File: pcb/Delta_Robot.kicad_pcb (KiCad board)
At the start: 2 copper layers, 95.5 x 69.6 mm, 136 parts, among them IC1 STMPS2151STR, J1 Conn_01x04, J2 Conn_01x03, J3 USB_A, J4 Conn_01x02, J5 Conn_01x02, J6 MP3V5050VC6U, J7 RJ45, J8 USB_OTG, J9 Conn_01x03, Q1 IRF9540STRLPBF, Q2 IRF9540STRLPBF, SW3 TL3305A, SW4 TL3305A, U2 LDL1117S33R, U3 ZLDO1117G12TA, U4 ICE40UP5K-SG48I, U5 W25Q64JVSSIQ, U6 STM32F412RGT6, U7 Omega2+, U8 4N25-X007T, U9 4N25-X007T, Y1 8MHz, Y2 32.768KHZ

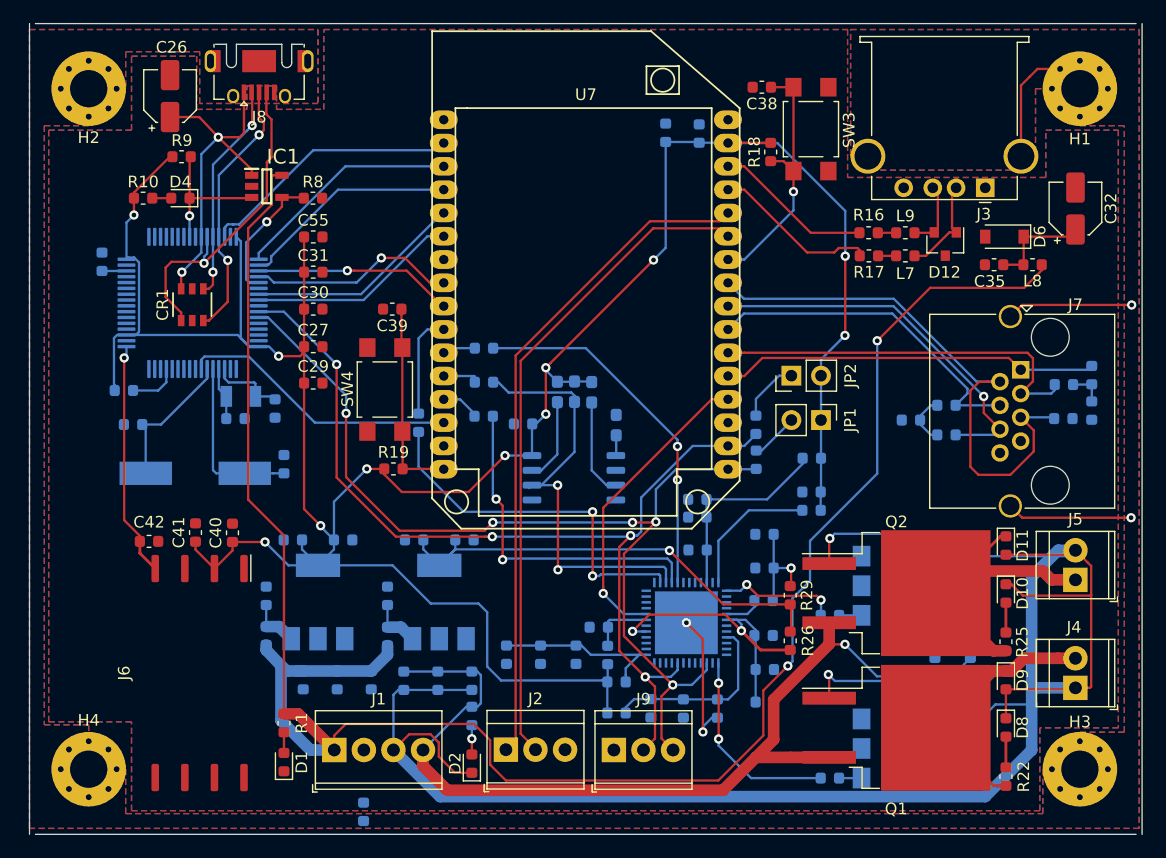
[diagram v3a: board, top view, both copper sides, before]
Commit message: Mejora footprint USB-A-B
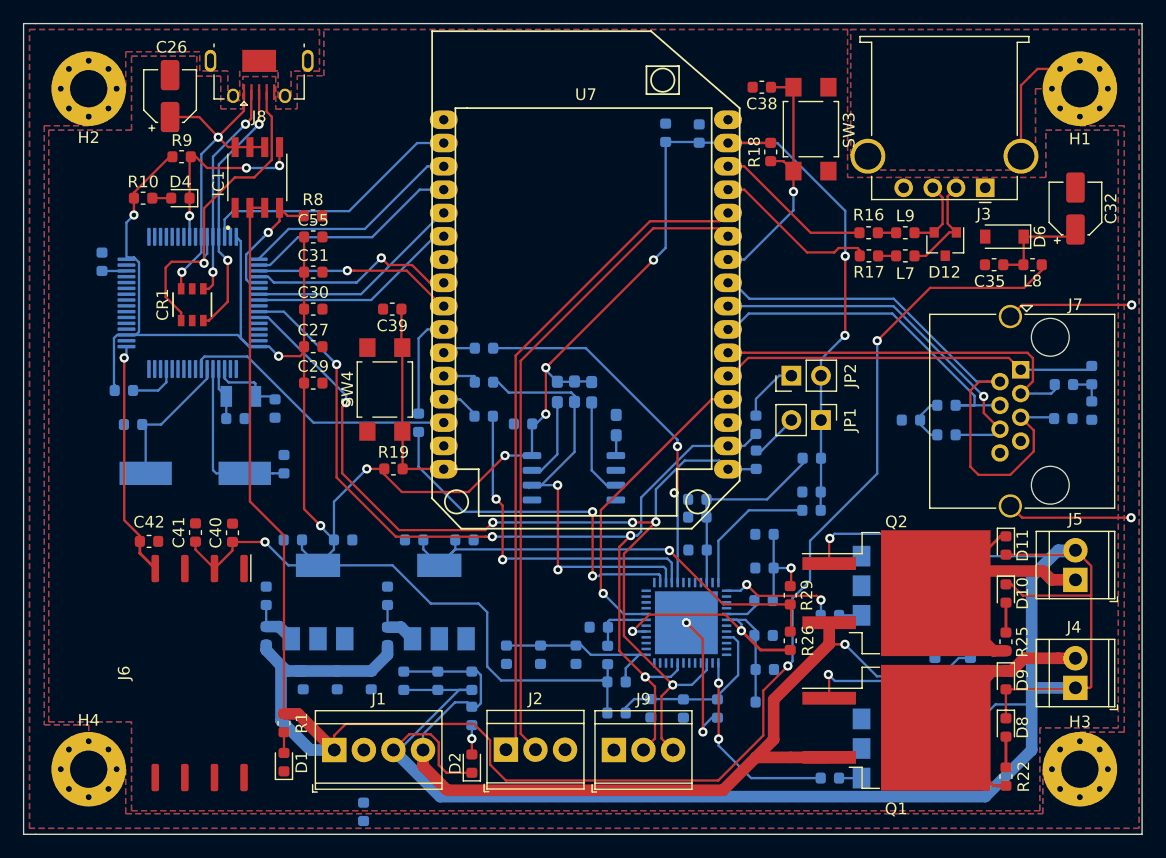
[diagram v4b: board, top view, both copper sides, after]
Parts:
- IC1: value STMPS2151STR -> STMPS2151MTR; footprint SMD:SOT95P280X145-5N -> SMD:SOIC127P600X175-8N
- J8: footprint Connector_USB:USB_Micro-AB_Molex_47590-0001 -> SMD:USB_Micro-AB_Molex_47590-0001
- moved R8 1.52 mm to (114.5, 73.2)
- moved IC1 1.11 mm to (109.7, 69.8), turned to 90 degrees
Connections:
- IC1 pad 1: /STM32/STM32_USB_VBUS -> GND
- IC1 pad 2: GND -> +5V
- IC1 pad 3: /STM32/STM32_USB_OverCurrent -> +5V
- IC1 pad 5: +5V -> /STM32/STM32_USB_OverCurrent
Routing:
- net /STM32/STM32_USB_OverCurrent: track 12.9 -> 17.2 mm, vias 1 -> 3
- net GNDPWR: track 153.6 -> 157.1 mm
- net +5V: track 177.4 -> 174.1 mm
- net Net-(Q1-Pad1): track 21.8 -> 23.9 mm
- net /Onion Omega 2/OMEGA2_ETH_TX+: track 29.5 -> 30.9 mm
- net /STM32/STM32_USB_VBUS: track 29.6 -> 28.4 mm
- net +24V: track 82.1 -> 83.2 mm
- net /External Communications/EXT_I2C1: track 85.5 -> 86.4 mm
- net /STM32/STM32_USB_ID: track 28.5 -> 29.3 mm
- net /FPGA/FPGA_VCCIO_O: track 16.1 -> 15.6 mm
- net /STM32/STM32_USB_PowerSwitchOn: track 11.4 -> 10.9 mm
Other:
- board size 95.5 x 69.6 mm -> 96 x 69.6 mm

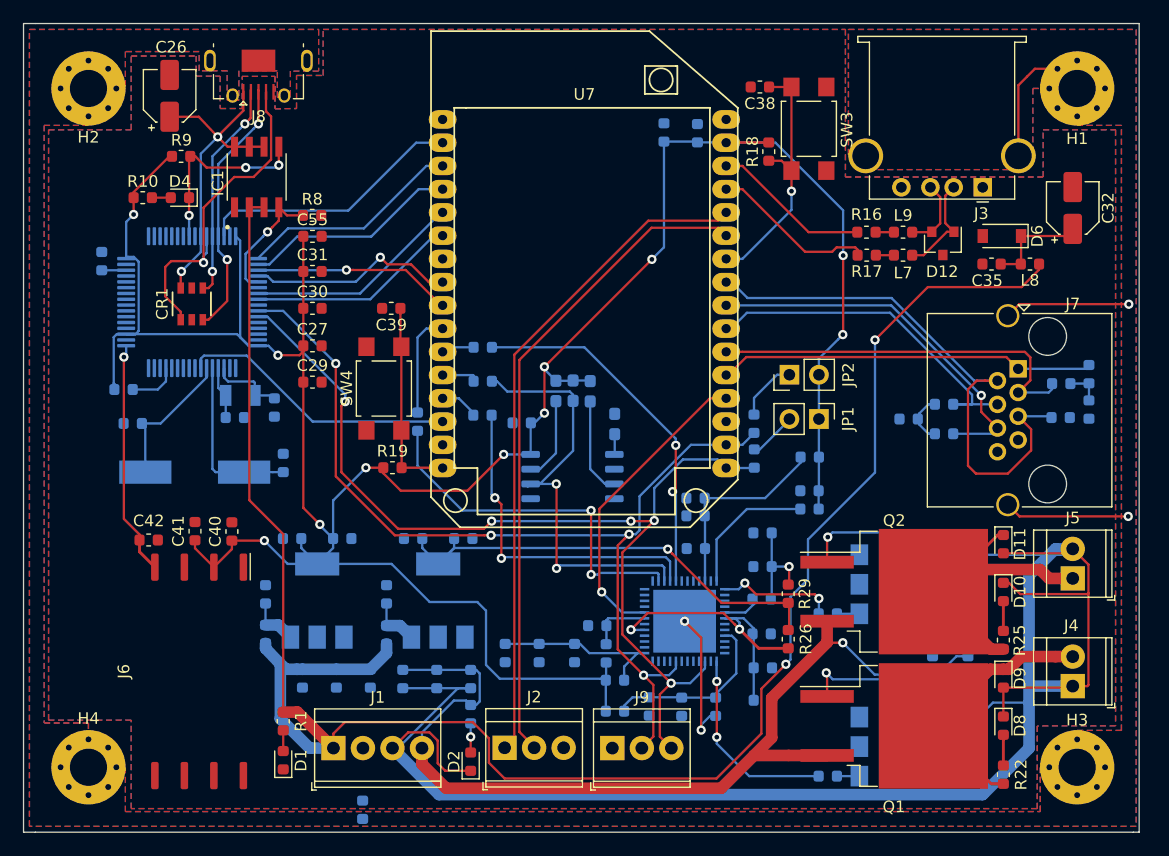
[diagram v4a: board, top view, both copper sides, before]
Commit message: Correccion UART Micro-Omega2
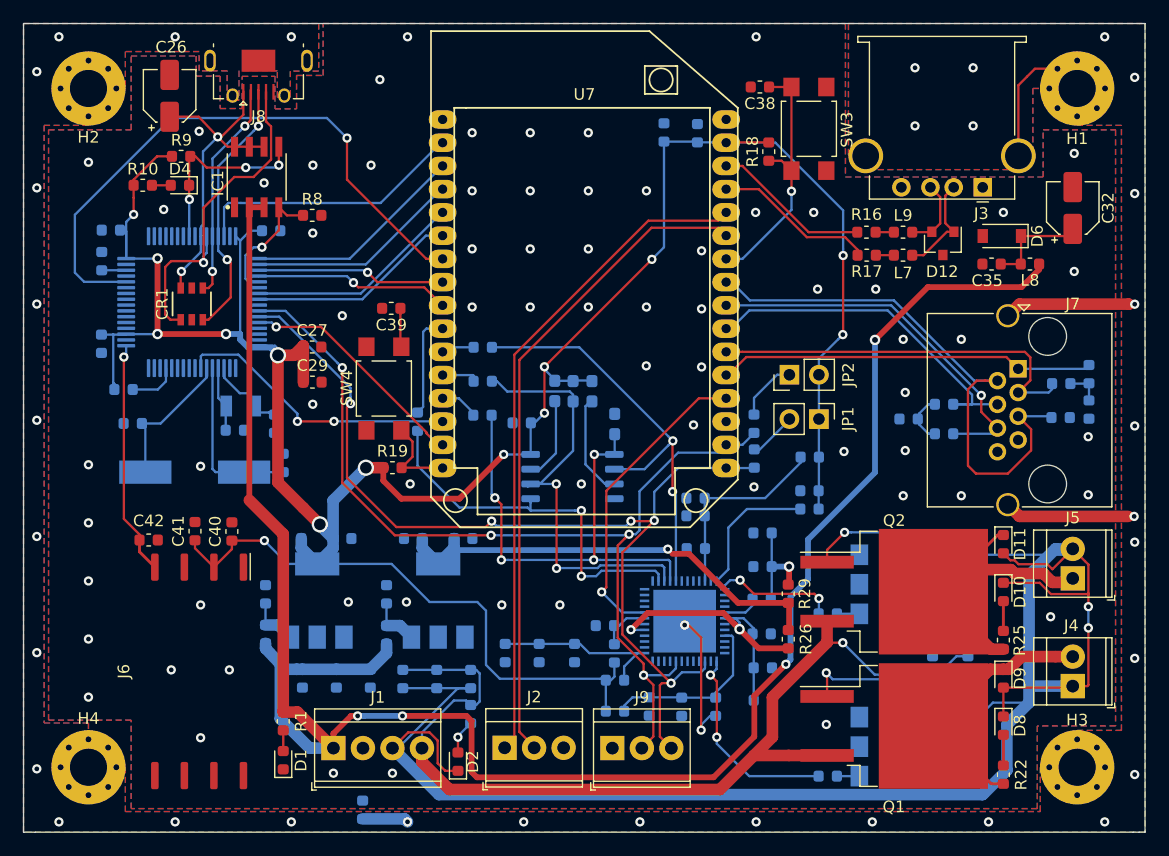
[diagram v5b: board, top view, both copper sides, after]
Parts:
- C30, C31, C55: moved to B.Cu
- moved C55 20.4 mm to (96.4, 84.2), turned to 270 degrees
- moved C31 17.7 mm to (97.2, 74.4), turned to 180 degrees
- moved C30 7.57 mm to (111.0, 74.5)
- moved C34 1.40 mm to (111.3, 91.1)
- moved C54 1.09 mm to (107.8, 91.6)
- moved D2 1.09 mm to (127.1, 120.2)
- moved D4 1.07 mm to (103.1, 70.6)
- moved R10 1.07 mm to (99.9, 70.6)
- moved Y2 0.92 mm to (108.4, 89.6)
- moved R28 0.71 mm to (140.5, 110.8)
- moved D5 0.66 mm to (139.7, 108.5)
- moved R5 0.15 mm to (138.6, 88.3)
- moved C27 0.10 mm to (114.5, 84.5)
- moved R6 0.10 mm to (135.4, 88.3)
- moved R3 0.05 mm to (137.0, 88.3)
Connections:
- R4 pad 1: Net-(R4-Pad1) -> /FPGA/FPGA_SPI3
- U5 pad 1: Net-(R4-Pad1) -> /FPGA/FPGA_SPI3
- U5 pad 2: (no net) -> /FPGA/FPGA_SPI1
- U5 pad 5: (no net) -> /FPGA/FPGA_SPI0
- U6 pad 28: (no net) -> /Onion Omega 2/STM32_BOOT1
- U6 pad 51: /Onion Omega 2/Omega2_SER1_TX -> /Onion Omega 2/Omega2_SER1_RX
- U6 pad 52: /Onion Omega 2/Omega2_SER1_RX -> /Onion Omega 2/Omega2_SER1_TX
- U6 pad 60: (no net) -> /Onion Omega 2/STM32_BOOT0
- U7 pad 15: (no net) -> /Onion Omega 2/STM32_BOOT0
- U7 pad 7: (no net) -> /Onion Omega 2/STM32_BOOT1
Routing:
- net /Onion Omega 2/STM32_BOOT1: track 0.00 -> 51.9 mm, vias 0 -> 1
- net /Onion Omega 2/STM32_BOOT0: track 0.00 -> 20.3 mm, vias 0 -> 1
- net /FPGA/FPGA_SPI3: track 29.1 -> 41.6 mm, vias 2 -> 4
- net +3V3: track 242.2 -> 249.4 mm, vias 11 -> 14
- net /Onion Omega 2/~OMEGA2_RST: track 18.2 -> 11.8 mm
- net /FPGA/FPGA_SPI1: track 31.6 -> 37.2 mm
- net GND_CASE: track 34.0 -> 38.0 mm, vias 2 -> 33
- net Net-(R4-Pad1): track 1.75 -> 0.00 mm
- net Net-(Q2-Pad1): track 24.2 -> 22.6 mm
- net /Onion Omega 2/Omega2_SER1_RX: track 17.8 -> 16.3 mm
- net +5V: track 174.1 -> 175.6 mm, vias 2 -> 4
- net /FPGA/FPGA_SPI0: track 31.6 -> 32.9 mm
- net Net-(C54-Pad1): track 4.52 -> 5.65 mm
- net /FPGA/FPGA_CDONE: track 5.44 -> 4.50 mm
- net /Onion Omega 2/OMEGA2_JTAG_TMS: track 23.0 -> 23.6 mm
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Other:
- board size 96 x 69.6 mm -> 96.5 x 69.6 mm
